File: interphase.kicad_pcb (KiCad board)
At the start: 2 copper layers, 49.5 x 10.8 mm, 115 parts, among them J1 Conn_01x04_Male, SW11 MOM-SPST, SW12 MOM-SPST, SW13 MOM-SPST, SW14 MOM-SPST, SW15 MOM-SPST, SW16 MOM-SPST, SW17 MOM-SPST, SW18 MOM-SPST, SW19 MOM-SPST, SW2 MOM-SPST, SW20 MOM-SPST, SW21 MOM-SPST, SW22 MOM-SPST, SW23 MOM-SPST, SW24 MOM-SPST, SW25 MOM-SPST, SW26 MOM-SPST, SW27 MOM-SPST, SW28 MOM-SPST, SW29 MOM-SPST, SW3 MOM-SPST, SW30 MOM-SPST, SW31 MOM-SPST, SW32 MOM-SPST, SW33 MOM-SPST, SW34 MOM-SPST, SW35 MOM-SPST, SW4 MOM-SPST, SW5 MOM-SPST, SW6 MOM-SPST, SW7 MOM-SPST, SW8 MOM-SPST, SW9 MOM-SPST, U1 Core51822B, U2 MCP1640, U3 MCP1640, U4 Core51822B

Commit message: prettify
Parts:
- J1: footprint Pin_Headers:Pin_Header_Angled_1x04_Pitch2.54mm -> Pin_Headers:Pin_Header_Straight_1x04_Pitch2.54mm
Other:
- board size 49.5 x 10.8 mm -> 142.2 x 132.1 mm
- board text added: "INTERPHASE"

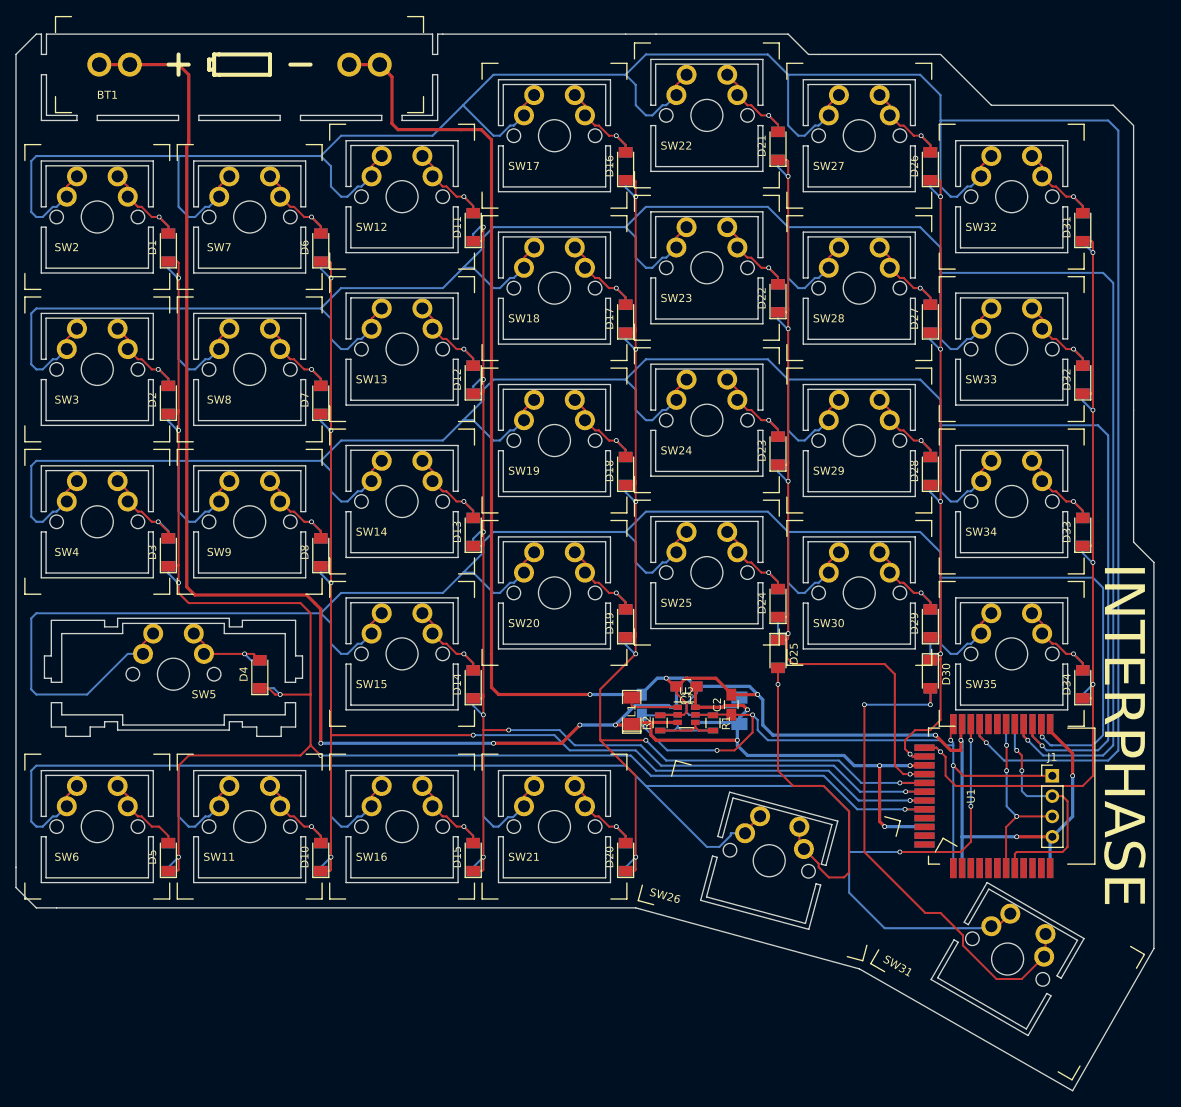
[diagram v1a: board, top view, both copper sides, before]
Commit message: finish layout and fix prototype issues
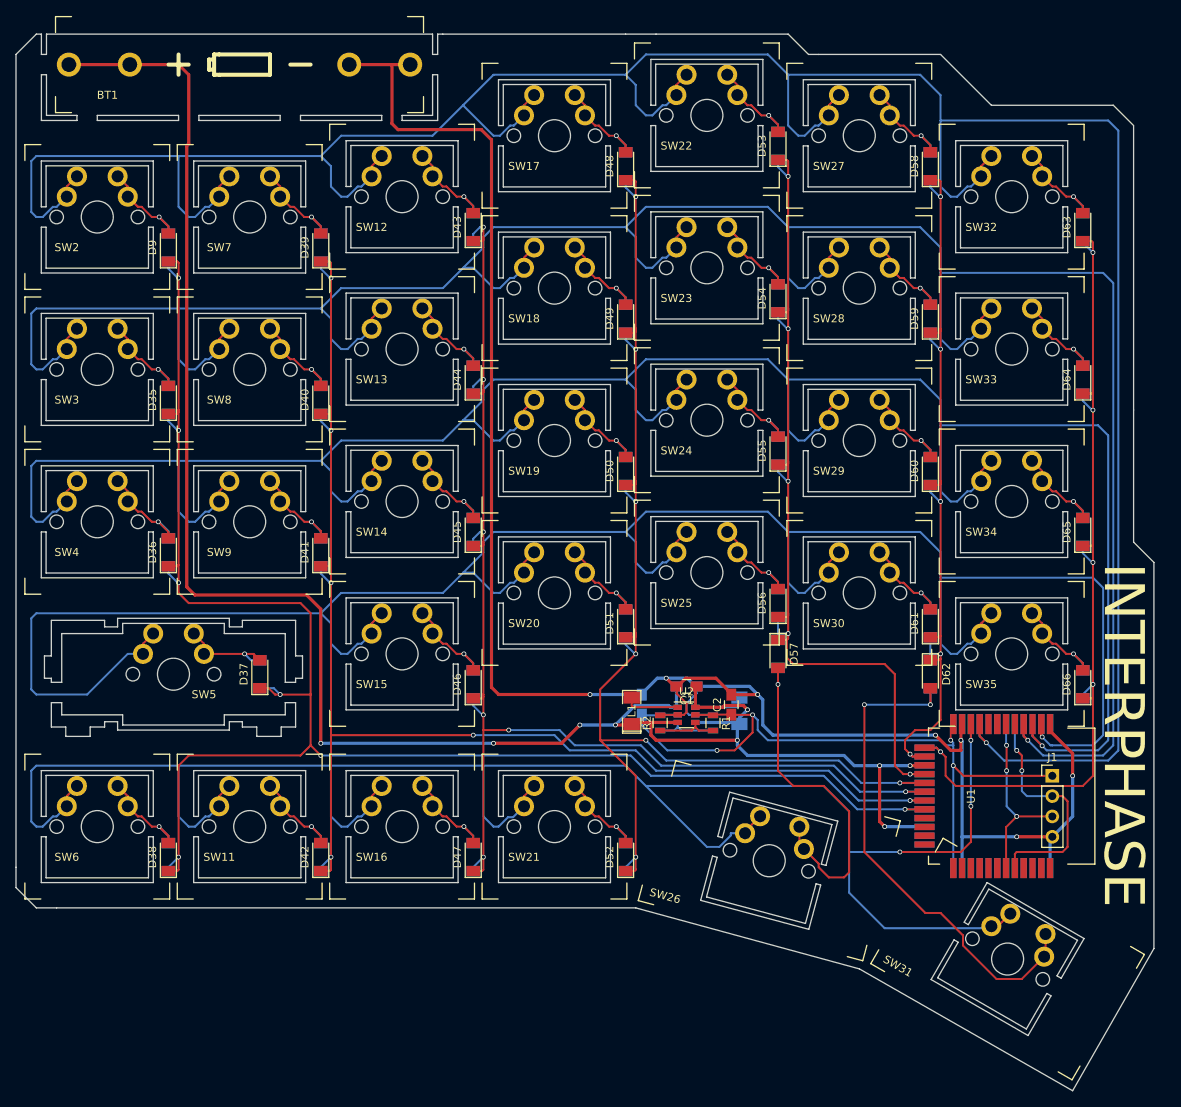
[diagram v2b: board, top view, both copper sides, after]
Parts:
- renumbered D2 to D35, D3 to D36, D4 to D37, D5 to D38, D6 to D39, D7 to D40, D8 to D41, D10 to D42, D11 to D43, D12 to D44, D13 to D45, D14 to D46, D15 to D47, D16 to D48, D17 to D49, D18 to D50, D19 to D51, D20 to D52, D21 to D53, D22 to D54, D23 to D55, D24 to D56, D25 to D57, D26 to D58, D27 to D59, D28 to D60, D29 to D61, D30 to D62, D31 to D63, D32 to D64, D33 to D65, D34 to D66, D1 to D9
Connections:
- D35 pad 1: Net-(D1-Pad1) -> Net-(D35-Pad1)
- D36 pad 1: Net-(D1-Pad1) -> Net-(D36-Pad1)
- D37 pad 1: Net-(D1-Pad1) -> Net-(D37-Pad1)
- D38 pad 1: Net-(D1-Pad1) -> Net-(D38-Pad1)
- D39 pad 1: Net-(D10-Pad1) -> Net-(D39-Pad1)
- D40 pad 1: Net-(D10-Pad1) -> Net-(D40-Pad1)
- D41 pad 1: Net-(D10-Pad1) -> Net-(D41-Pad1)
- D42 pad 1: Net-(D10-Pad1) -> Net-(D42-Pad1)
- D43 pad 1: Net-(D11-Pad1) -> Net-(D43-Pad1)
- D44 pad 1: Net-(D11-Pad1) -> Net-(D44-Pad1)
- D45 pad 1: Net-(D11-Pad1) -> Net-(D45-Pad1)
- D46 pad 1: Net-(D11-Pad1) -> Net-(D46-Pad1)
- D47 pad 1: Net-(D11-Pad1) -> Net-(D47-Pad1)
- D48 pad 1: Net-(D16-Pad1) -> Net-(D48-Pad1)
- D49 pad 1: Net-(D16-Pad1) -> Net-(D49-Pad1)
- D50 pad 1: Net-(D16-Pad1) -> Net-(D50-Pad1)
- D51 pad 1: Net-(D16-Pad1) -> Net-(D51-Pad1)
- D52 pad 1: Net-(D16-Pad1) -> Net-(D52-Pad1)
- D53 pad 1: Net-(D21-Pad1) -> Net-(D53-Pad1)
- D54 pad 1: Net-(D21-Pad1) -> Net-(D54-Pad1)
- D55 pad 1: Net-(D21-Pad1) -> Net-(D55-Pad1)
- D56 pad 1: Net-(D21-Pad1) -> Net-(D56-Pad1)
- D57 pad 1: Net-(D21-Pad1) -> Net-(D57-Pad1)
- D58 pad 1: Net-(D26-Pad1) -> Net-(D58-Pad1)
- D59 pad 1: Net-(D26-Pad1) -> Net-(D59-Pad1)
- D60 pad 1: Net-(D26-Pad1) -> Net-(D60-Pad1)
- D61 pad 1: Net-(D26-Pad1) -> Net-(D61-Pad1)
- D62 pad 1: Net-(D26-Pad1) -> Net-(D62-Pad1)
- D63 pad 1: Net-(D31-Pad1) -> Net-(D63-Pad1)
- D64 pad 1: Net-(D31-Pad1) -> Net-(D64-Pad1)
- D65 pad 1: Net-(D31-Pad1) -> Net-(D65-Pad1)
- D66 pad 1: Net-(D31-Pad1) -> Net-(D66-Pad1)
- D9 pad 1: Net-(D1-Pad1) -> Net-(D9-Pad1)
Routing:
- net Net-(D1-Pad1): track 213.8 -> 208.1 mm
- net Net-(D11-Pad1): track 161.4 -> 155.7 mm
- net Net-(D26-Pad1): track 98.0 -> 92.5 mm
- net Net-(D16-Pad1): track 156.0 -> 150.5 mm
- net Net-(D21-Pad1): track 113.3 -> 107.8 mm
- net Net-(D10-Pad1): track 171.4 -> 166.8 mm
- net Net-(D31-Pad1): track 109.3 -> 104.9 mm
- net +BATT: track 237.8 -> 241.6 mm
- net GND: track 237.8 -> 241.0 mm
- net Net-(D38-Pad2): track 11.1 -> 13.6 mm, vias 0 -> 1
- net Net-(D42-Pad1): track 0.00 -> 1.34 mm
- net Net-(D38-Pad1): track 0.00 -> 1.34 mm
- net Net-(D47-Pad1): track 0.00 -> 1.34 mm
- net Net-(D62-Pad1): track 0.00 -> 1.10 mm
- net Net-(D61-Pad1): track 0.00 -> 1.10 mm
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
